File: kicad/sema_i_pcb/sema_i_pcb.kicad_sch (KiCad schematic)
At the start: 14 parts, among them J1 Conn_01x02_Pin, J2 Conn_01x02_Pin, J3 Conn_01x04_Pin, U1 PIC24FJ64GA002-I_SP, U2 ESP8266-01_ESP-01

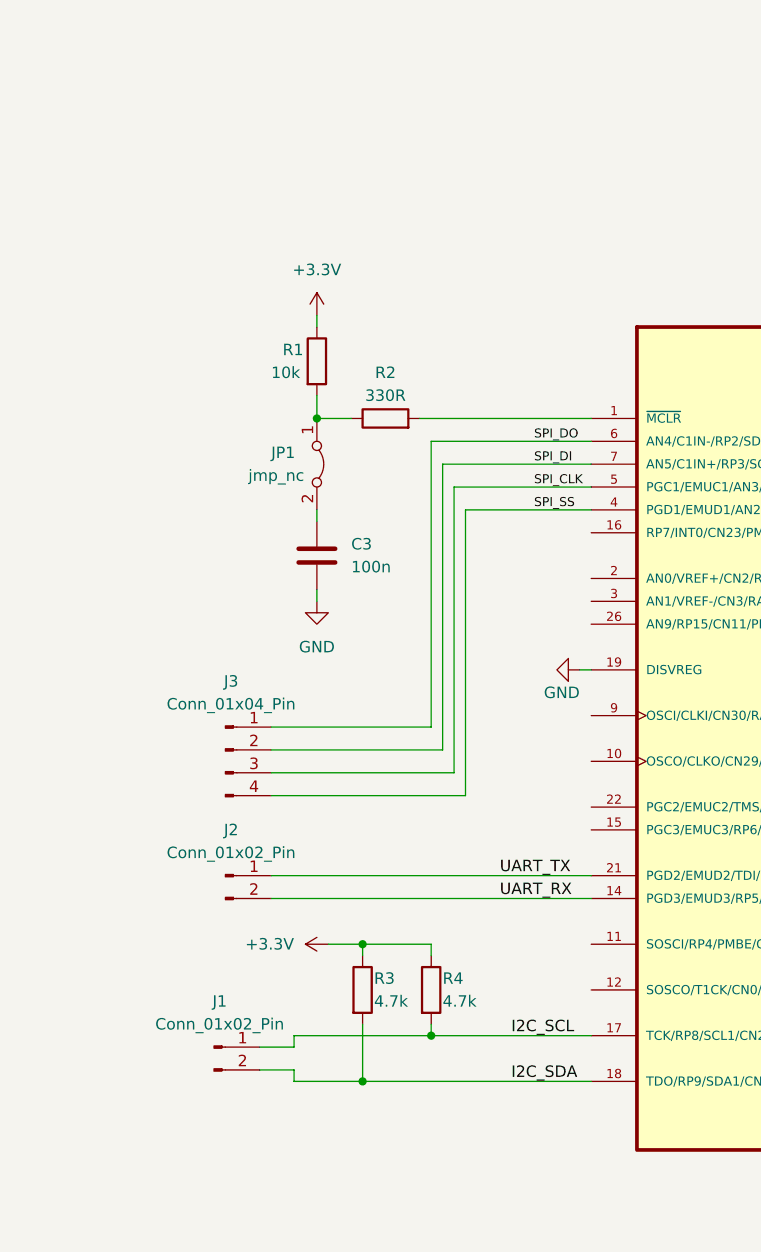
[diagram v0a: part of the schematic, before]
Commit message: Issue #4 : Planiranje projektovanja električne šeme
- Modifikovani folderi tako da se obezbjedi laksi uvoz modela
- Modifikovana sema da se omoguci programiranje flash memorije
- Dodatne izmjene na semi
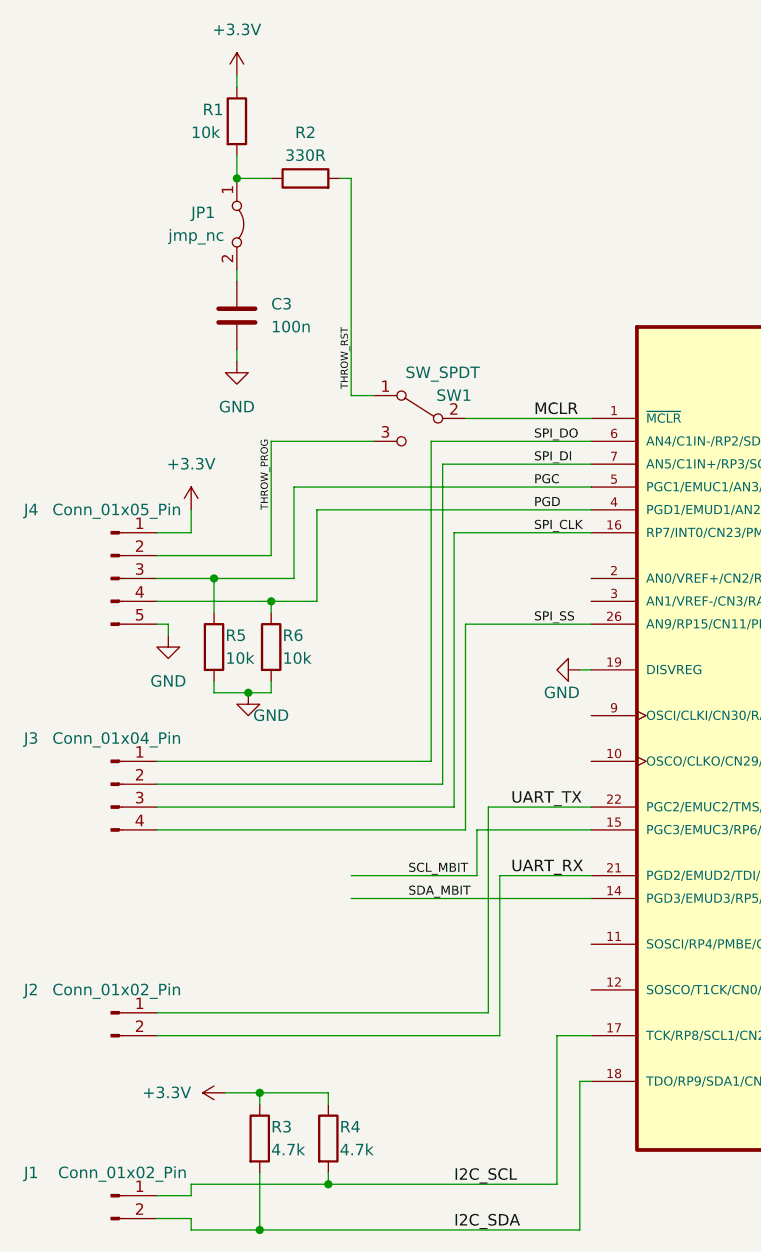
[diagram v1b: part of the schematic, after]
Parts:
- added J4: Conn_01x05_Pin, symbol Connector:Conn_01x05_Pin
- added R5, R6: 10k, symbol Device:R
- added SW1: SW_SPDT, symbol Switch:SW_SPDT
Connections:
- net +3.3V: now also J4.1 (Pin_1)
- net GND: now also J4.5 (Pin_5), R5.2, R6.2
- net SPI_CLK: now also U1.16 (RP7/INT0/CN23/PMD5/RB7); no longer U1.5 (PGC1/EMUC1/AN3/C2IN+/RP1/CN5/RB1)
- net SPI_SS: now also U1.26 (AN9/RP15/CN11/PMCS1/RB15); no longer U1.4 (PGD1/EMUD1/AN2/C2IN-/RP0/CN4/RB0)
- net UART_RX: now also U1.21 (PGD2/EMUD2/TDI/RP10/CN16/PMD2/RB10); no longer U1.14 (PGD3/EMUD3/RP5/ASDA1/CN27/PMD7/RB5)
- net UART_TX: now also U1.22 (PGC2/EMUC2/TMS/RP11/CN15/PMD1/RB11); no longer U1.21 (PGD2/EMUD2/TDI/RP10/CN16/PMD2/RB10)
- net MCLR: now reaches U1.1 (~{MCLR})
- net MCLR: now also SW1.2 (B); no longer R2.2
- net SCL_MBIT: now reaches U1.15 (PGC3/EMUC3/RP6/ASCL1/CN24/PMD6/RB6)
- new net PGC: J4.3 (Pin_3), R5.1, U1.5 (PGC1/EMUC1/AN3/C2IN+/RP1/CN5/RB1)
- new net PGD: J4.4 (Pin_4), R6.1, U1.4 (PGD1/EMUD1/AN2/C2IN-/RP0/CN4/RB0)
- new net SDA_MBIT: U1.14 (PGD3/EMUD3/RP5/ASDA1/CN27/PMD7/RB5)
- new net THROW_PROG: J4.2 (Pin_2), SW1.3 (C)
- new net THROW_RST: R2.2, SW1.1 (A)
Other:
- moved on the sheet: C3, J1, J2, J3, JP1, R1, R2, R3, R4

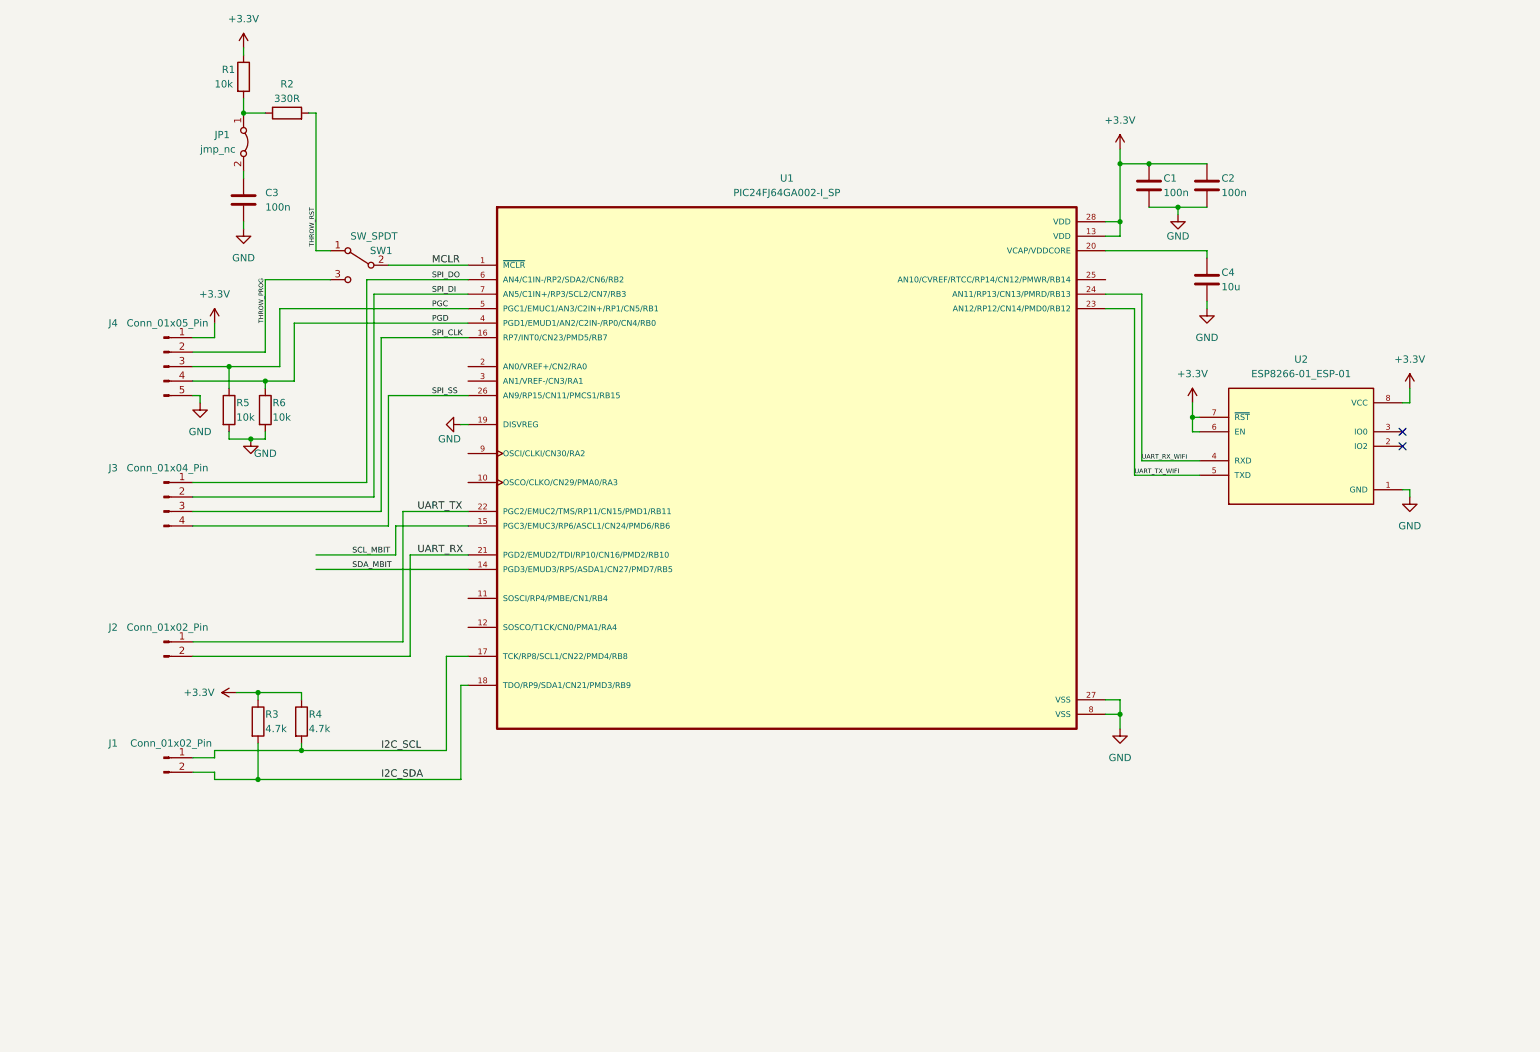
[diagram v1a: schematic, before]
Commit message: Issue #4 : Planiranje projektovanja električne šeme
- Dodan dio za napajanje, sa DC/DC pretvaračem
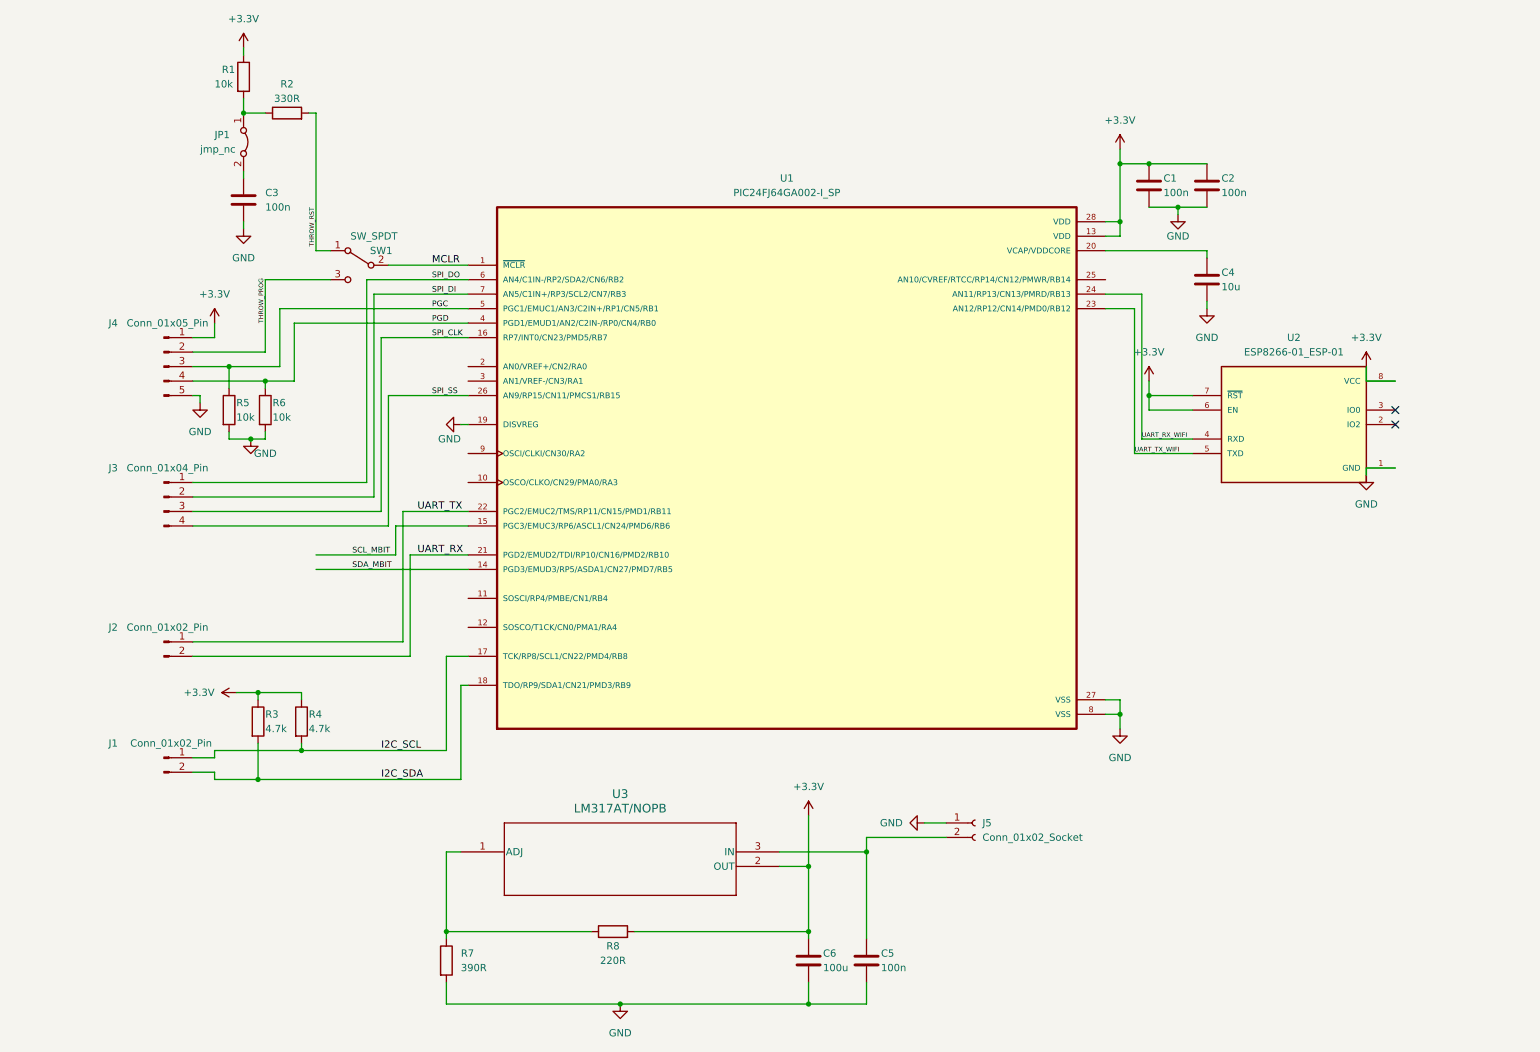
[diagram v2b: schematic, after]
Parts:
- added C5: 100n, symbol Device:C
- added C6: 100u, symbol Device:C
- added J5: Conn_01x02_Socket, symbol Connector:Conn_01x02_Socket
- added R7: 390R, symbol Device:R
- added R8: 220R, symbol Device:R
- added U3: LM317AT/NOPB, T03B_TEX, symbol LM317AT:LM317AT_NOPB
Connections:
- net +3.3V: now also C6.2, R8.2, U3.2 (OUT)
- net GND: now also C5.2, C6.1, J5.1 (Pin_1), R7.2
- new net: R7.1, R8.1, U3.1 (ADJ)
- new net: C5.1, J5.2 (Pin_2), U3.3 (IN)
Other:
- moved on the sheet: U2

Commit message: Issue #4 : Planiranje projektovanja električne šeme
- Reorganizovana šema i izvršena ERC provjera
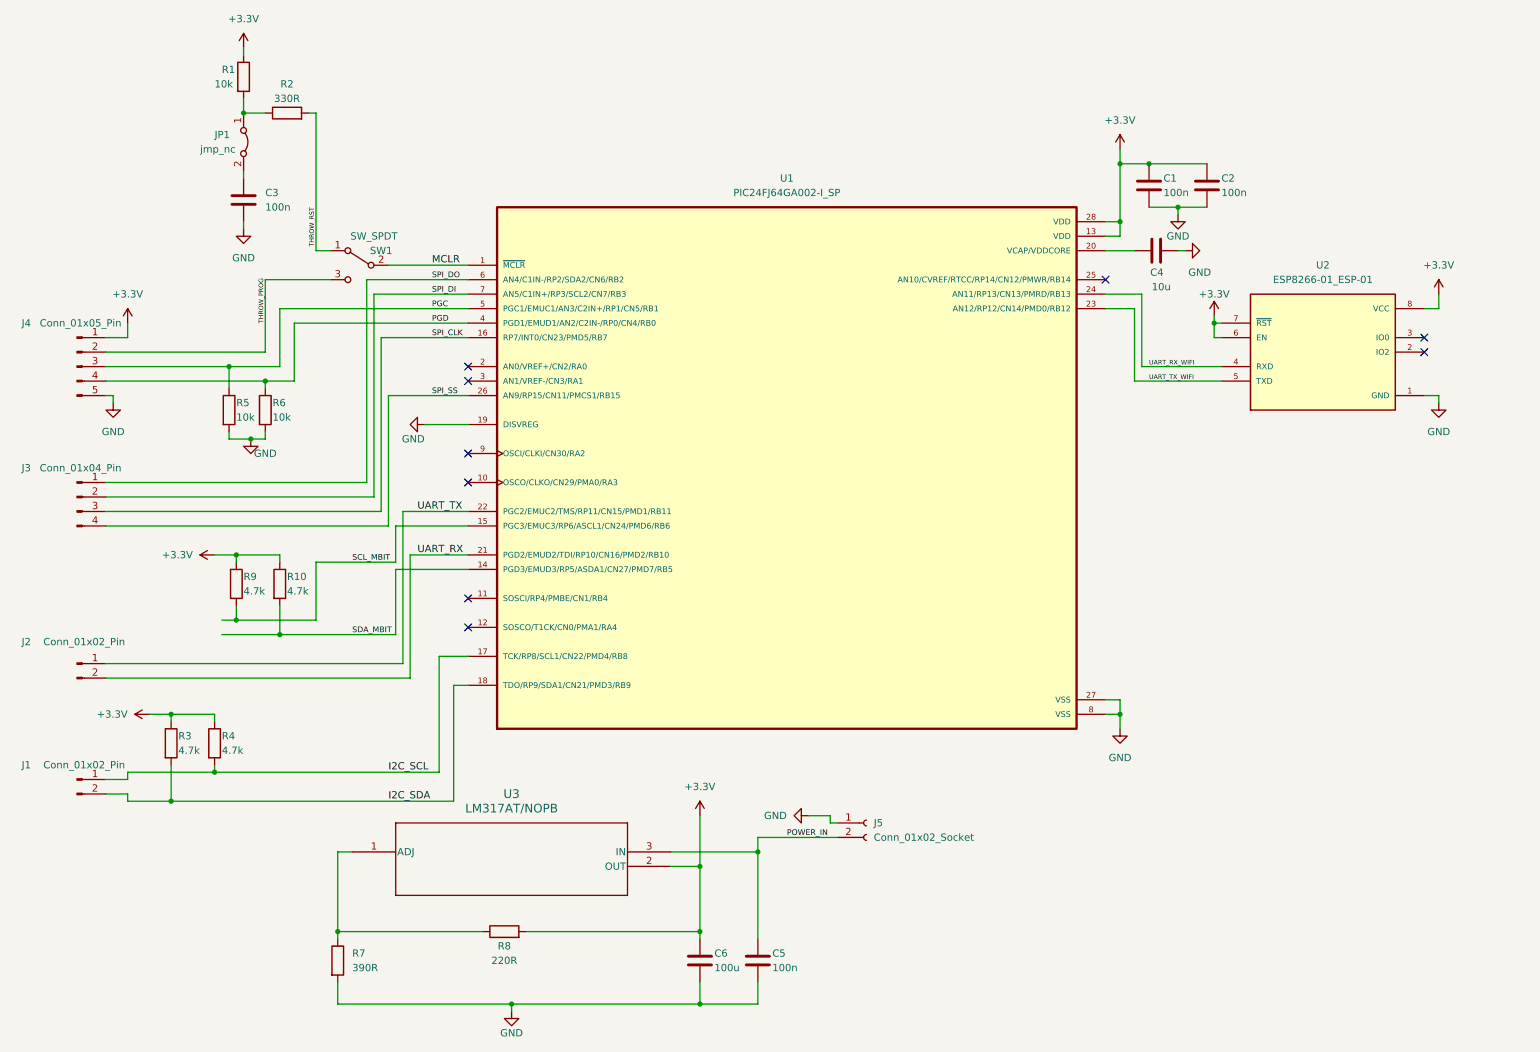
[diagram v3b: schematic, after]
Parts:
- added R10, R9: 4.7k, symbol Device:R
- U1: footprint PIC24FJ64GA002-I_SP:DIP787W46P254L3467H508Q28 -> MCU:DIP787W46P254L3467H508Q28
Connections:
- net +3.3V: now also R10.1, R9.1
- net SCL_MBIT: now also R9.2
- net SDA_MBIT: now also R10.2
- net POWER_IN: now reaches C5.1, J5.2 (Pin_2), U3.3 (IN)
- no-connect marks 2 -> 9
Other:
- moved on the sheet: C4, C5, C6, J1, J2, J3, J4, J5, R3, R4, R7, R8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

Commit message: Issue #4 : Projektovanje električne šeme
- Uklonjen dio sa DC/DC pretvaračem zbog napajanja sa postojeće ploče
- Dodan sprežni kondezator između napajanja i mase kod WiFi modula
- Umjesto jumpera ubačen taster kod kola za reset MCRL pina
- Dodatne modifikacije i poboljšanja
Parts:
- removed C6: 100u, symbol Device:C
- removed J5: Conn_01x02_Socket, symbol Connector:Conn_01x02_Socket
- removed JP1: jmp_nc, symbol Jumper:Jumper_2_Bridged
- removed R7: 390R, symbol Device:R
- removed R8: 220R, symbol Device:R
- removed U3: LM317AT/NOPB, T03B_TEX, symbol LM317AT:LM317AT_NOPB
- added SW2: SW_Push, Button_Switch_THT:SW_PUSH-12mm, symbol Switch:SW_Push
- renumbered J1 to I2C, J4 to PICkit_Conn, J3 to SPI, J2 to UART
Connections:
- net POWER_IN is gone; now on net +3.3V: C5.1
- net at C3.1: now also SW2.1
- net at R1.2, R2.1: now also SW2.2
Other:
- moved on the sheet: R2
